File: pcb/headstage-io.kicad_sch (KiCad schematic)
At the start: 4 parts, among them J2 BTE-040-03-L-D-A, J3 BTE-040-03-L-D-A

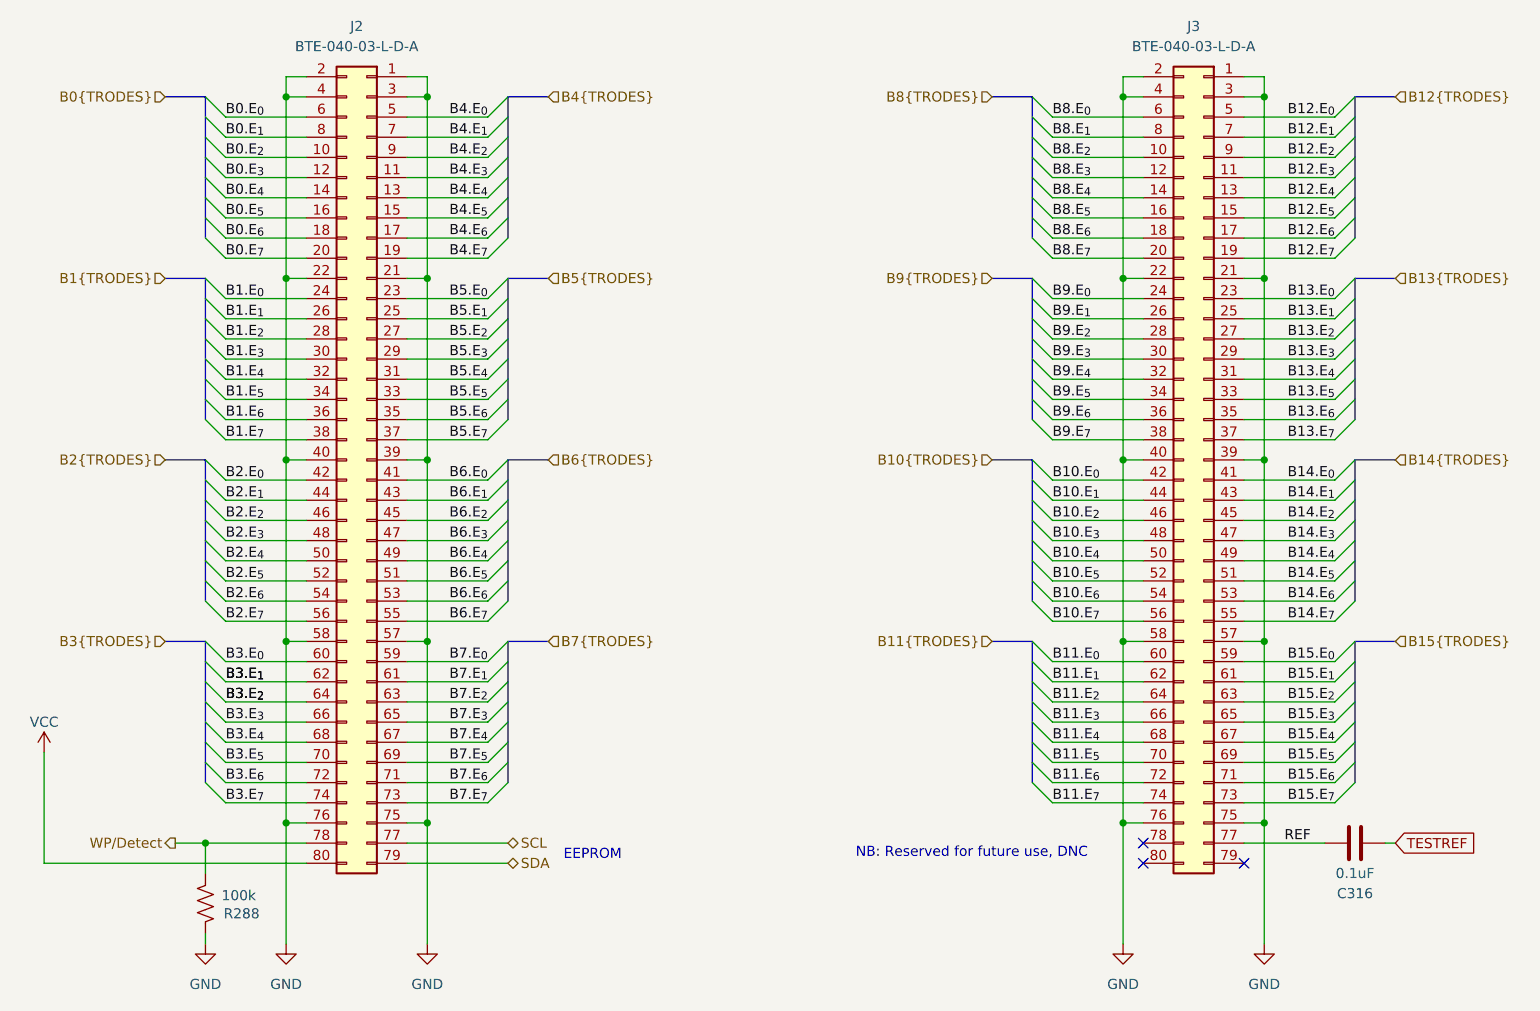
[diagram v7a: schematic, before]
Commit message: Implmenent bipolar test signal
- Generate internal negative rail
- Shift DAC output by VREF/2
- Replace analog switches with depletion mode switches to allow negative
  signals
- DC couple electrode inputs
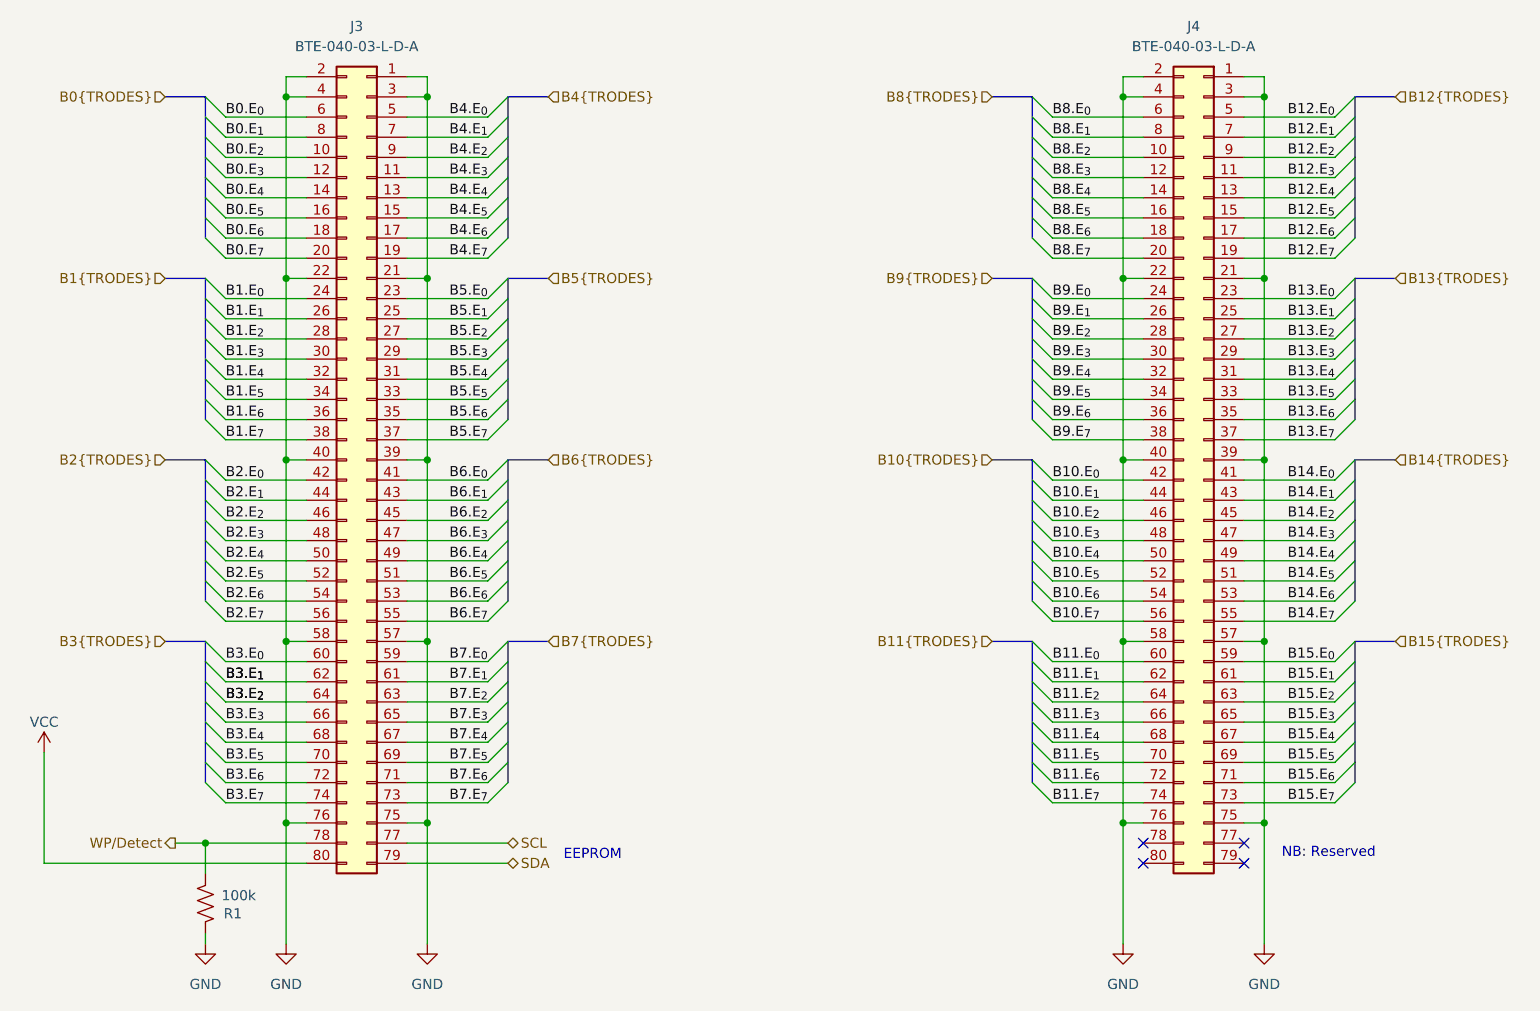
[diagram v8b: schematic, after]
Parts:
- removed C316: 0.1uF, Capacitor_SMD:C_0402_1005Metric, symbol Device:C
- renumbered J2 to J3, J3 to J4, R288 to R1
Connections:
- net REF: no longer names the net of J4.77 (Pin_77)
- no-connect marks 3 -> 4
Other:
- note added: "NB: Reserved"
- note removed: "NB: Reserved for future use, DNC"
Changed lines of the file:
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@@
 	(title_block
 		(title "Extracellular Electrophysiology Test Board")
-		(rev "E")
+		(rev "F")
 		(company "Open Ephys, Inc")
 		(comment 1 "Jonathan P. Newman")
@@
 		)
 	)
-	(text "NB: Reserved for future use, DNC"
+	(text "NB: Reserved"
 		(exclude_from_sim no)
-		(at 165.1 142.24 0)
+		(at 210.058 142.24 0)
 		(effects
 			(font
@@
 	)
 	(no_connect
-		(at 186.69 140.97)
+		(at 199.39 140.97)
 	)
 	(no_connect
-		(at 186.69 143.51)
+		(at 199.39 143.51)
 	)
 	(no_connect
-		(at 199.39 143.51)
+		(at 186.69 140.97)
+	)
+	(no_connect
+		(at 186.69 143.51)
 	)
 	(bus_entry
@@
 		)
 	)
-	(wire
-		(pts
-			(xy 184.15 138.43) (xy 184.15 153.67)
-		)
-		(stroke
-			(width 0)
-			(type default)
-		)
-	)
 	(bus
 		(pts
@@
 	(wire
 		(pts
+			(xy 184.15 138.43) (xy 184.15 153.67)
+		)
+		(stroke
+			(width 0)
+			(type default)
+		)
+	)
+	(wire
+		(pts
 			(xy 175.26 80.01) (xy 186.69 80.01)
 		)
@@
 	(wire
 		(pts
-			(xy 199.39 140.97) (xy 209.55 140.97)
-		)
-		(stroke
-			(width 0)
-			(type default)
-		)
-	)
-	(wire
-		(pts
 			(xy 71.12 118.11) (xy 81.28 118.11)
 		)
@@
 	(wire
 		(pts
-			(xy 217.17 140.97) (xy 218.44 140.97)
-		)
-		(stroke
-			(width 0)
-			(type default)
-		)
-	)
-	(wire
-		(pts
 			(xy 199.39 123.19) (xy 210.82 123.19)
 		)
@@
 		)
 	)
-	(label "REF"
-		(at 204.47 140.97 0)
-		(effects
-			(font
-				(size 1.27 1.27)
-			)
-			(justify left bottom)
-		)
-	)
 	(label "B8.E_{7}"
 		(at 175.26 67.31 0)
@@
 		)
 	)
-	(global_label "TESTREF"
-		(shape input)
-		(at 218.44 140.97 0)
-		(fields_autoplaced yes)
-		(effects
-			(font
-				(size 1.27 1.27)
-			)
-			(justify left)
-		)
-		(property "Intersheetrefs" "${INTERSHEET_REFS}"
-			(at 229.2265 140.97 0)
-			(effects
-				(font
-					(size 1.27 1.27)
-				)
-				(justify left)
-				(hide yes)
-			)
-		)
-	)
 	(hierarchical_label "B0{TRODES}"
 		(shape input)
@@
 		(dnp no)
 		(fields_autoplaced yes)
-		(property "Reference" "#PWR0763"
+		(property "Reference" "#PWR010"
 			(at 68.58 160.02 0)
 			(effects
@@
 			(project "ephys-test-board"
 				(path "/ffaa6ffd-73fa-4da3-9ff1-78fa7369281f/f2c6d928-7acb-4b4d-942a-bf07e4ec8d7a"
-					(reference "#PWR0763")
+					(reference "#PWR010")
 					(unit 1)
 				)
@@
 		(dnp no)
 		(fields_autoplaced yes)
-		(property "Reference" "#PWR04"
+		(property "Reference" "#PWR013"
 			(at 184.15 160.02 0)
 			(effects
@@
 			(project "ephys-test-board"
 				(path "/ffaa6ffd-73fa-4da3-9ff1-78fa7369281f/f2c6d928-7acb-4b4d-942a-bf07e4ec8d7a"
-					(reference "#PWR04")
-					(unit 1)
-				)
-			)
-		)
-	)
-	(symbol
-		(lib_id "Device:C")
-		(at 213.36 140.97 270)
-		(unit 1)
-		(exclude_from_sim no)
-		(in_bom yes)
-		(on_board yes)
-		(dnp no)
-		(property "Reference" "C316"
-			(at 213.36 147.32 90)
-			(effects
-				(font
-					(size 1.27 1.27)
-				)
-			)
-		)
-		(property "Value" "0.1uF"
-			(at 213.36 144.78 90)
-			(effects
-				(font
-					(size 1.27 1.27)
-				)
-			)
-		)
-		(property "Footprint" "Capacitor_SMD:C_0402_1005Metric"
-			(at 209.55 141.9352 0)
-			(effects
-				(font
-					(size 1.27 1.27)
-				)
-				(hide yes)
-			)
-		)
-		(property "Datasheet" "~"
-			(at 213.36 140.97 0)
-			(effects
-				(font
-					(size 1.27 1.27)
-				)
-				(hide yes)
-			)
-		)
-		(property "Description" "Unpolarized capacitor"
-			(at 213.36 140.97 0)
-			(effects
-				(font
-					(size 1.27 1.27)
-				)
-				(hide yes)
-			)
-		)
-		(property "TempCo" "X7R"
-			(at 213.36 140.97 0)
-			(effects
-				(font
-					(size 1.27 1.27)
-				)
-				(hide yes)
-			)
-		)
-		(property "Voltage" "25V"
-			(at 213.36 140.97 0)
-			(effects
-				(font
-					(size 1.27 1.27)
-				)
-				(hide yes)
-			)
-		)
-		(property "Datasheet1" ""
-			(at 213.36 140.97 0)
-			(effects
-				(font
-					(size 1.27 1.27)
-				)
-				(hide yes)
-			)
-		)
-		(property "Part No." ""
-			(at 213.36 140.97 0)
-			(effects
-				(font
-					(size 1.27 1.27)
-				)
-				(hide yes)
-			)
-		)
-		(property "Tolerance" ""
-			(at 213.36 140.97 0)
-			(effects
-				(font
-					(size 1.27 1.27)
-				)
-			)
-		)
-		(property "MPN" "C1005X7R1E104K050BB"
-			(at 213.36 140.97 0)
-			(effects
-				(font
-					(size 1.27 1.27)
-				)
-				(hide yes)
-			)
-		)
-		(property "OEPSPN" "OEPS010050"
-			(at 213.36 140.97 0)
-			(effects
-				(font
-					(size 1.27 1.27)
-				)
-				(hide yes)
-			)
-		)
-		(property "LCSC" "C105883"
-			(at 213.36 140.97 90)
-			(effects
-				(font
-					(size 1.27 1.27)
-				)
-				(hide yes)
-			)
-		)
-		(pin "1"
-		)
-		(pin "2"
-		)
-		(instances
-			(project "ephys-test-board"
-				(path "/ffaa6ffd-73fa-4da3-9ff1-78fa7369281f/f2c6d928-7acb-4b4d-942a-bf07e4ec8d7a"
-					(reference "C316")
+					(reference "#PWR013")
 					(unit 1)
 				)
@@
 		(dnp no)
 		(fields_autoplaced yes)
-		(property "Reference" "#PWR03"
+		(property "Reference" "#PWR012"
 			(at 96.52 160.02 0)
 			(effects
@@
 			(project "ephys-test-board"
 				(path "/ffaa6ffd-73fa-4da3-9ff1-78fa7369281f/f2c6d928-7acb-4b4d-942a-bf07e4ec8d7a"
-					(reference "#PWR03")
+					(reference "#PWR012")
 					(unit 1)
 				)
@@
 		(on_board yes)
 		(dnp no)
-		(property "Reference" "R288"
+		(property "Reference" "R1"
 			(at 70.866 149.86 0)
 			(effects
@@
 			(project "ephys-test-board"
 				(path "/ffaa6ffd-73fa-4da3-9ff1-78fa7369281f/f2c6d928-7acb-4b4d-942a-bf07e4ec8d7a"
-					(reference "R288")
+					(reference "R1")
 					(unit 1)
 				)
@@
 		(on_board yes)
 		(dnp no)
-		(property "Reference" "#PWR0774"
+		(property "Reference" "#PWR09"
 			(at 48.26 133.35 0)
 			(effects
@@
 			(project "ephys-test-board"
 				(path "/ffaa6ffd-73fa-4da3-9ff1-78fa7369281f/f2c6d928-7acb-4b4d-942a-bf07e4ec8d7a"
-					(reference "#PWR0774")
+					(reference "#PWR09")
 					(unit 1)
 				)
@@
 		(on_board yes)
 		(dnp no)
-		(property "Reference" "J3"
+		(property "Reference" "J4"
 			(at 193.04 38.1 0)
 			(effects
@@
 			(project "ephys-test-board"
 				(path "/ffaa6ffd-73fa-4da3-9ff1-78fa7369281f/f2c6d928-7acb-4b4d-942a-bf07e4ec8d7a"
-					(reference "J3")
+					(reference "J4")
 					(unit 1)
 				)
@@
 		(dnp no)
 		(fields_autoplaced yes)
-		(property "Reference" "#PWR02"
+		(property "Reference" "#PWR011"
 			(at 78.74 160.02 0)
 			(effects
@@
 			(project "ephys-test-board"
 				(path "/ffaa6ffd-73fa-4da3-9ff1-78fa7369281f/f2c6d928-7acb-4b4d-942a-bf07e4ec8d7a"
-					(reference "#PWR02")
+					(reference "#PWR011")
 					(unit 1)
 				)
@@
 		(dnp no)
 		(fields_autoplaced yes)
-		(property "Reference" "#PWR05"
+		(property "Reference" "#PWR014"
 			(at 201.93 160.02 0)
 			(effects
@@
 			(project "ephys-test-board"
 				(path "/ffaa6ffd-73fa-4da3-9ff1-78fa7369281f/f2c6d928-7acb-4b4d-942a-bf07e4ec8d7a"
-					(reference "#PWR05")
+					(reference "#PWR014")
 					(unit 1)
 				)
@@
 		(on_board yes)
 		(dnp no)
-		(property "Reference" "J2"
+		(property "Reference" "J3"
 			(at 87.63 38.1 0)
 			(effects
@@
 			(project "ephys-test-board"
 				(path "/ffaa6ffd-73fa-4da3-9ff1-78fa7369281f/f2c6d928-7acb-4b4d-942a-bf07e4ec8d7a"
-					(reference "J2")
+					(reference "J3")
 					(unit 1)
 				)
